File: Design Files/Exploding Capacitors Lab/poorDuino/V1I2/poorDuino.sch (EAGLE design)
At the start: 30 parts, among them IC1 LD117AS33TR, IC2 LD117AS50TR, X1 POWERSUPPLY_DC21MMX, Y2 CSTCE16M0V53-R0 16MHZ

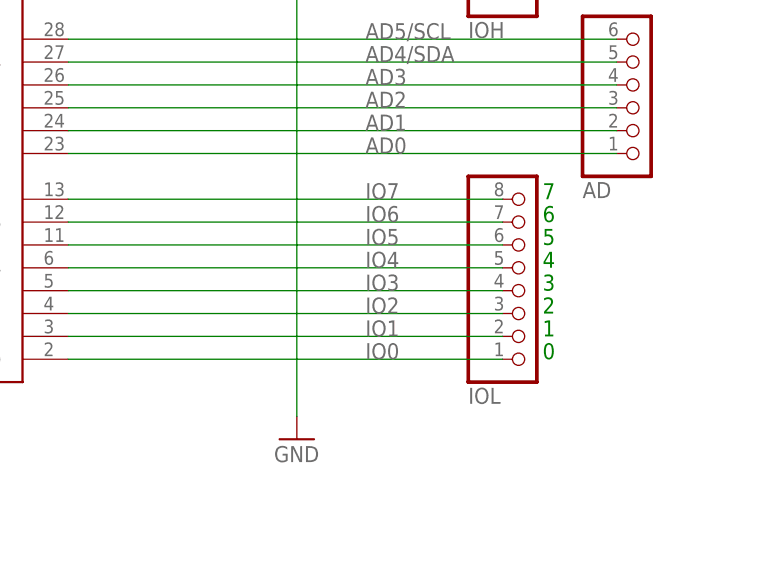
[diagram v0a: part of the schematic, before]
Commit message: Differential pair routing applied to traces related to V-USB support (DIO2 and DIO4)
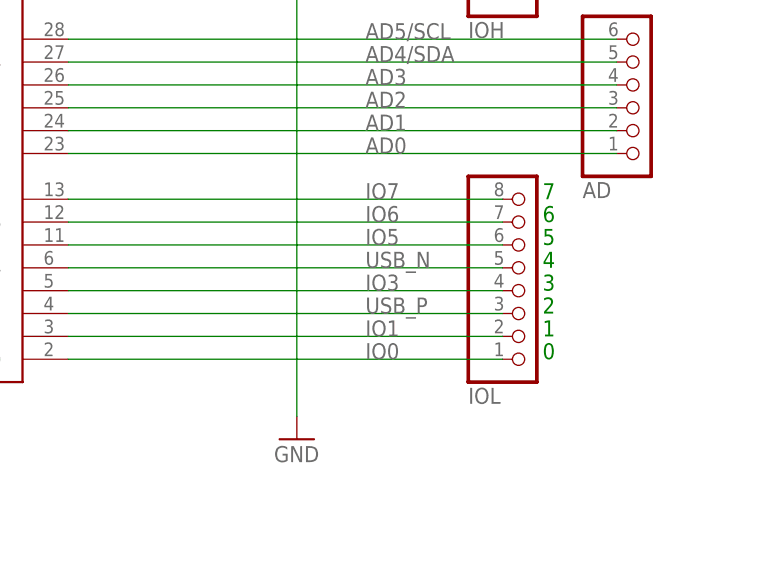
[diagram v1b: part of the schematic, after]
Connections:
- net IO2 renamed USB_P
- net IO4 renamed USB_N
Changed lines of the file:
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@@
 </segment>
 </net>
-<net name="IO2" class="0">
+<net name="USB_P" class="0">
 <segment>
 <wire x1="234.95" y1="81.28" x2="186.69" y2="81.28" width="0.1524" layer="91"/>
@@
 </segment>
 </net>
-<net name="IO4" class="0">
+<net name="USB_N" class="0">
 <segment>
 <wire x1="234.95" y1="86.36" x2="186.69" y2="86.36" width="0.1524" layer="91"/>
